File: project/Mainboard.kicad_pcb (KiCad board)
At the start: 2 copper layers, 160 x 160 mm, 84 parts, among them IC1 74HC138, IC10 FT232RL, IC11 TL7702A, IC2 W65C02, IC3 74HC00, IC4 SYSTEM ROM, IC5 W65C22, IC6 RAM, IC7 W65C22, IC8 W65C51, IC9 74HC148, M1 R-785.0-1.0, SW1 CARRIER, SW2 PORT B, SW3 INTERRUPT, SW4 CLOCK INPUT, SW5 NMI, SW6 FT232 RESET, SW7 RESET, T1 BC546, X1 PORT B, X2 EXPANSION, X3 TIMER, X4 KEYBOARD, X5 EXT. CLOCK, X6 SERIAL, X7 GND, X8 DC IN

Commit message: Fix grid issues, fix missing libraries, replace FT232 with FT231
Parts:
- removed IC10: FT232RL, Package_SO:SSOP-28_5.3x10.2mm_P0.65mm
- added IC701: FT231XS, Package_SO:SSOP-20_3.9x8.7mm_P0.635mm, F.Cu at (280.6, 169.4)
- C301: renamed from C9; value 100nF -> 100n
- C501: renamed from C1; value 100nF -> 100n
- C502: renamed from C2; value 100nF -> 100n
- C503: renamed from C3; value 100nF -> 100n
- C504: renamed from C4; value 100nF -> 100n
- C505: renamed from C5; value 100nF -> 100n
- C506: renamed from C6; value 100nF -> 100n
- C507: renamed from C7; value 100nF -> 100n
- C508: renamed from C8; value 30pF -> 30p
- C601: renamed from C13; value 330nF -> 330n
- C602: renamed from C14; value 100nF -> 100n
- C603: renamed from C15; value 100nF -> 100n
- C604: renamed from C16; value 100nF -> 100n
- C605: renamed from C17; value 100nF -> 100n
- C606: renamed from C18; value 100nF -> 100n
- C701: renamed from C10; value 100nF -> 100n
- C702: renamed from C11; value 100nF -> 100n
- C703: renamed from C12; value 100nF -> 100n
- D601: renamed from D11; footprint Diode_THT:D_DO-35_SOD27_P7.62mm_Horizontal -> Diode_SMD:D_SOD-123
- R603: renamed from R12; value 470 -> 470R
- RN202: renamed from RN2; value 390 -> 390R
- SW601: renamed from SW6; value FT232 RESET -> FT231 RESET
- X501: renamed from X5; footprint Connector_Coaxial:MMCX_Molex_73415-1471_Vertical -> Connector_Coaxial:SMA_Amphenol_901-144_Vertical
- X602: renamed from X8; footprint Connector_Generic:BarrelJack_Wuerth_6941xx301002 -> Connector_BarrelJack:BarrelJack_Wuerth_6941xx301002
- moved X501 65.7 mm to (152.3, 161.4), turned to -90 degrees
- moved C701 9.91 mm to (282.8, 175.1)
- moved C703 9.14 mm to (276.0, 168.1), turned to -90 degrees
- moved C702 8.05 mm to (285.1, 169.4), turned to 90 degrees
- moved D601 5.84 mm to (154.6, 62.5)
- moved C602 0.21 mm to (263.5, 170.4)
- moved SW501 0.16 mm to (225.5, 158.9)
- renumbered D1 to D201, D2 to D202, D3 to D203, D4 to D204, D5 to D205, D6 to D206, D7 to D207, D8 to D208, D12 to D602, D9 to D701, D10 to D702, DS1 to DS401, IC9 to IC301, IC1 to IC501, IC2 to IC502, IC3 to IC503, IC4 to IC504, IC5 to IC505, IC6 to IC506, IC7 to IC507, IC8 to IC508, IC11 to IC601, M1 to M601, R6 to R301, R7 to R302, R1 to R401, R2 to R402, R3 to R403, R4 to R501, R5 to R502, R10 to R601, R11 to R602, R13 to R604, R14 to R605, R15 to R606, R8 to R701, R9 to R702, RN1 to RN201, RN3 to RN301, RV1 to RV401, SW1 to SW201, SW2 to SW202, SW3 to SW203, SW5 to SW301, SW4 to SW501, SW7 to SW602, T1 to T401, X1 to X201, X2 to X202, X3 to X401, X4 to X402, X7 to X601, X6 to X701, XTAL1 to XTAL501, XTAL2 to XTAL502
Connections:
- net /Supply/~{Reset_FT232} renamed /Supply/~{Reset_FT231}
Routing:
- net /Processor/CLOCK_EXT: track 6.93 -> 69.2 mm
- net /Processor/RxD: track 38.8 -> 24.3 mm, vias 2 -> 1
- net GND: track 37.2 -> 26.3 mm, vias 5 -> 3
- net /Processor/~{DSR}: track 52.2 -> 42.3 mm
- net /USB/D-: track 14.3 -> 7.06 mm
- net /USB/D+: track 14.3 -> 9.33 mm
- net /Processor/~{RTS}: track 37.4 -> 33.2 mm, vias 2 -> 0
- net +VDC: track 22.1 -> 18.0 mm
- net /Supply/~{Reset_FT231}: track 31.3 -> 27.7 mm
- net /Processor/~{DTR}: track 30.7 -> 27.4 mm
- net +5V: track 36.9 -> 34.1 mm
- net Net-(IC701-CBUS2): track 18.8 -> 21.3 mm
- net Net-(IC701-CBUS1): track 20.3 -> 18.3 mm, vias 0 -> 2
- net Net-(IC701-3V3OUT): track 3.73 -> 5.14 mm
- net /Processor/~{CTS}: track 30.3 -> 31.7 mm, vias 0 -> 2
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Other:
- board text added: "CONTRAST"

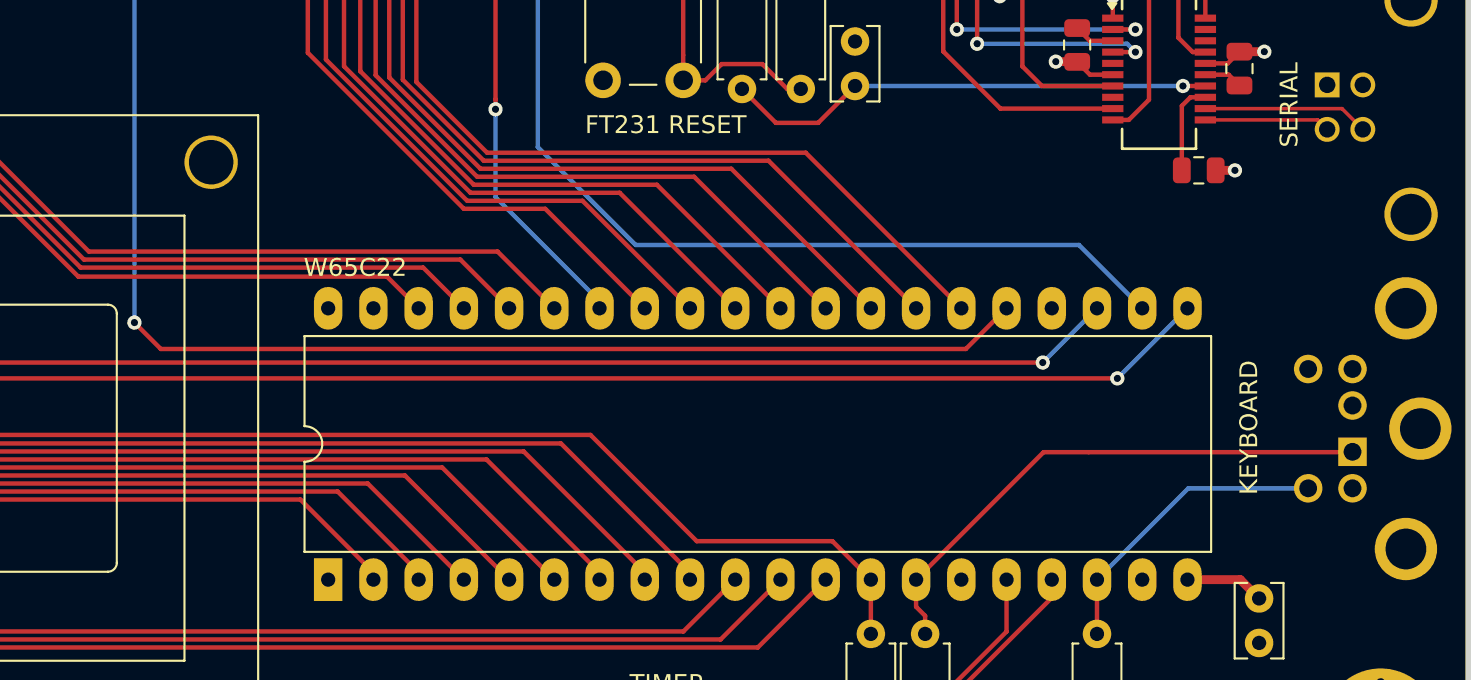
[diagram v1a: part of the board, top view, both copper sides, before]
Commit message: Fix swapped DM and DP, add missing datasheets, remove Mouser property
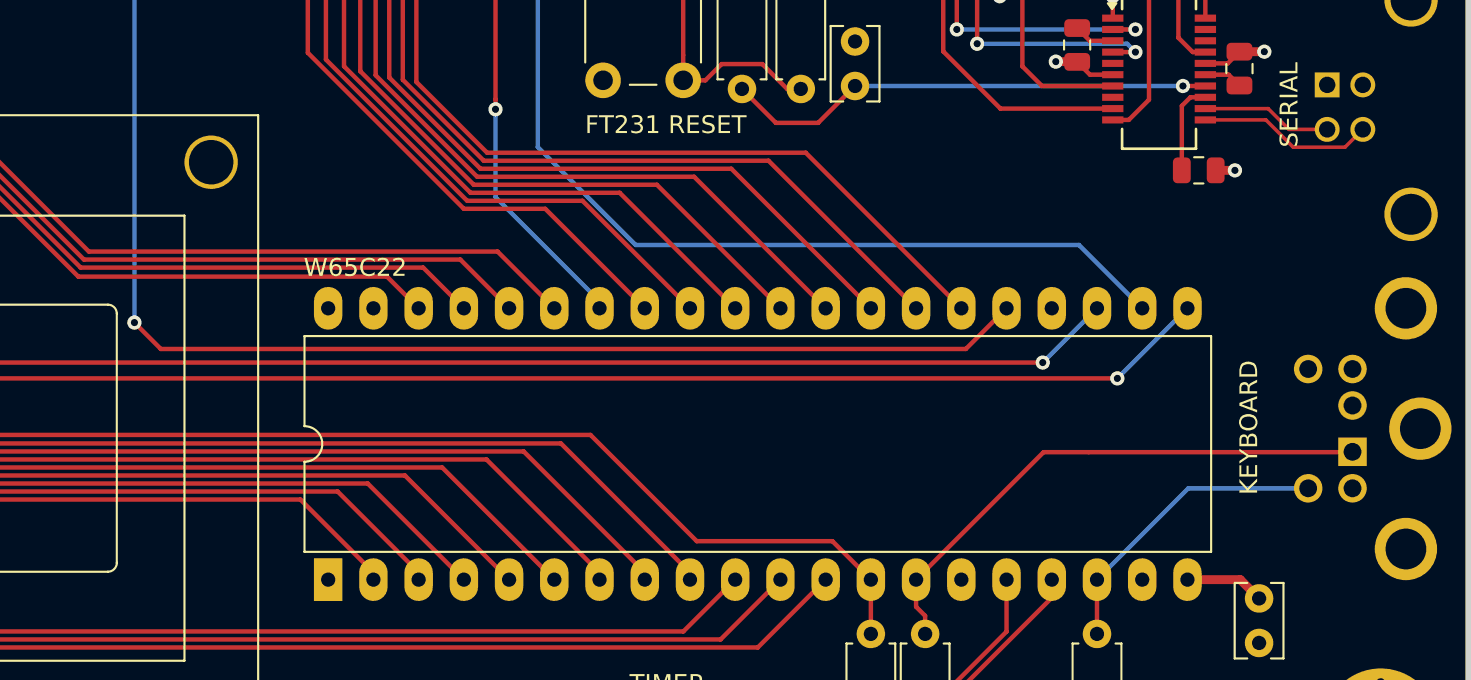
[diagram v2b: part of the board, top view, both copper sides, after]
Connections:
- IC701 pad 11: /USB/D- -> /USB/D+
- IC701 pad 12: /USB/D+ -> /USB/D-
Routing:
- net /USB/D+: track 9.33 -> 9.89 mm
